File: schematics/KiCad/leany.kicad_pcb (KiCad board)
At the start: 2 copper layers, 108.3 x 71.6 mm, 59 parts, among them J1 SWD, J2 ST7735S, J3 USB C, Q1 DMG6601LVT-7, SW1 BOOT_MODE, SW2 ZERO, SW3 HOLD, SW4 POWER, U1 LSM6DSO, U2 STM32F103C8Tx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

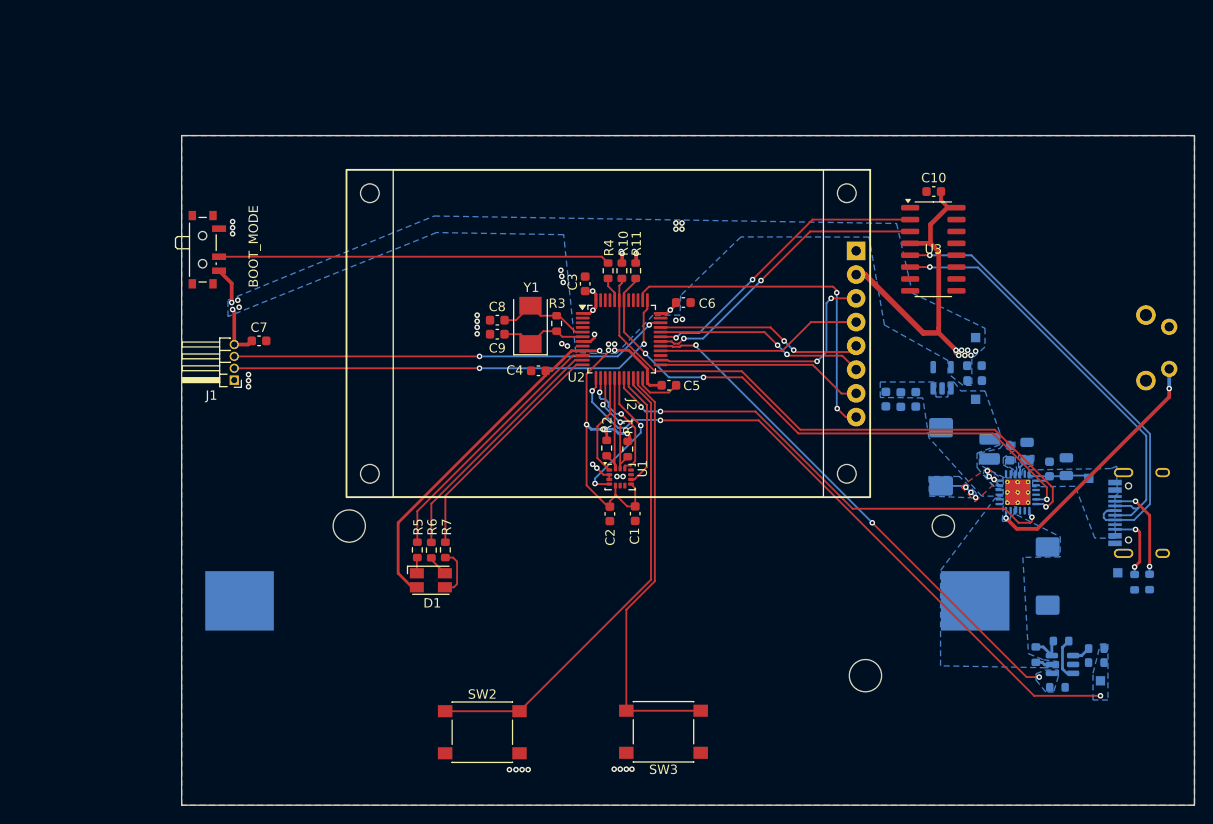
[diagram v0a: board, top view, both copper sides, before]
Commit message: add a mosfet to drive the ST7735S backlight fix copper zones
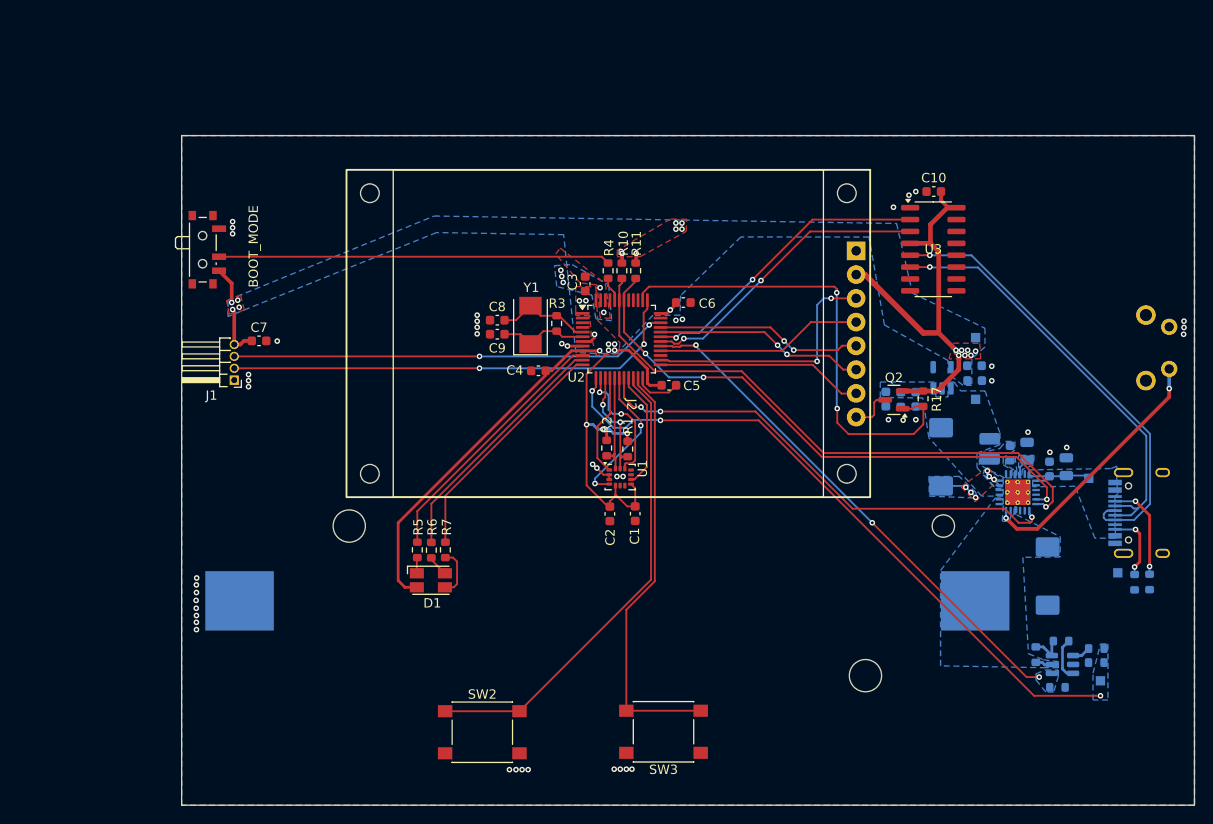
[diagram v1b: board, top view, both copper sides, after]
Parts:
- added Q2: AO3401A, Package_TO_SOT_SMD:SOT-23, F.Cu at (182.3, 96.8)
- added R17: 18k, Resistor_SMD:R_0603_1608Metric, F.Cu at (185.4, 96.6)
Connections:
- J2 pad 8: /ST7735S_BL -> Net-(J2-Pin_8)
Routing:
- net /ST7735S_BL: track 37.0 -> 50.6 mm
- net +3V3: track 134.2 -> 138.9 mm
- net Net-(J2-Pin_8): track 0.00 -> 4.65 mm
- net GND: track 14.2 -> 15.8 mm, vias 35 -> 60
- net /LSM6DSO_CS: track 12.7 -> 13.4 mm
- added copper zone on F.Cu, net +3V3

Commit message: add mounting holes and trademark
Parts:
- moved C11 20.8 mm to (178.0, 90.0)
- moved C13 20.8 mm to (184.0, 91.4)
- moved C17 20.8 mm to (167.9, 84.2)
- moved C2 20.8 mm to (135.2, 96.5)
- moved C4 20.8 mm to (127.6, 81.2)
- moved C5 20.8 mm to (141.5, 82.7)
- moved J1 20.8 mm to (95.1, 82.2)
- moved R17 20.8 mm to (168.7, 84.2)
- moved R3 20.8 mm to (129.5, 76.1)
- moved R4 20.8 mm to (135.0, 70.5)
- moved SW2 20.8 mm to (121.6, 119.8)
- moved SW4 20.8 mm to (195.0, 81.0)
- moved TP1 20.8 mm to (174.3, 84.2)
- moved TP2 20.8 mm to (186.4, 92.7)
- moved U4 20.8 mm to (170.8, 81.9)
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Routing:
- net (no net): vias 0 -> 4
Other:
- board text added: "Leany"
- board text added: "v0.1"
